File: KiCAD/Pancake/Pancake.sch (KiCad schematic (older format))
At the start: 44 parts, among them IC3 LF347N, J1 Conn_01x08_Male, J101 TB001-500-04BE, J102 TB001-500-03BE, J2 Conn_01x08_Male, J3 Conn_01x08_Male, J4 Conn_01x08_Male, J5 Conn_01x08_Male, J7 Conn_02x15_Top_Bottom

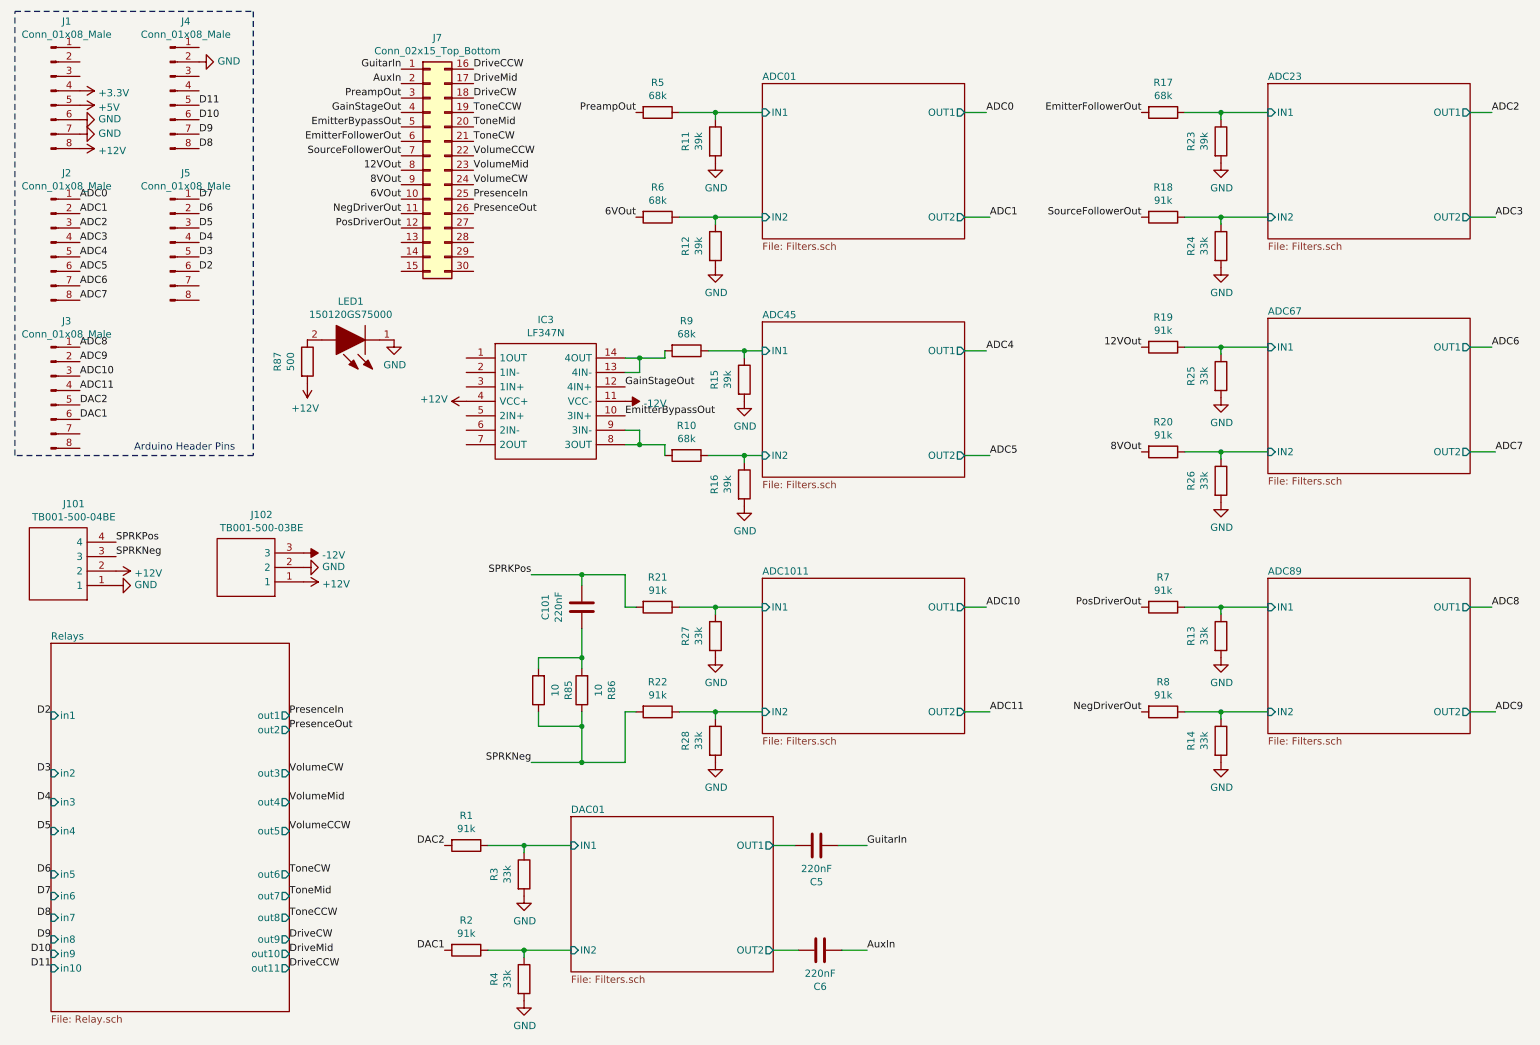
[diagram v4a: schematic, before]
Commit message: Will need to retrace in order to be built at SDSU.
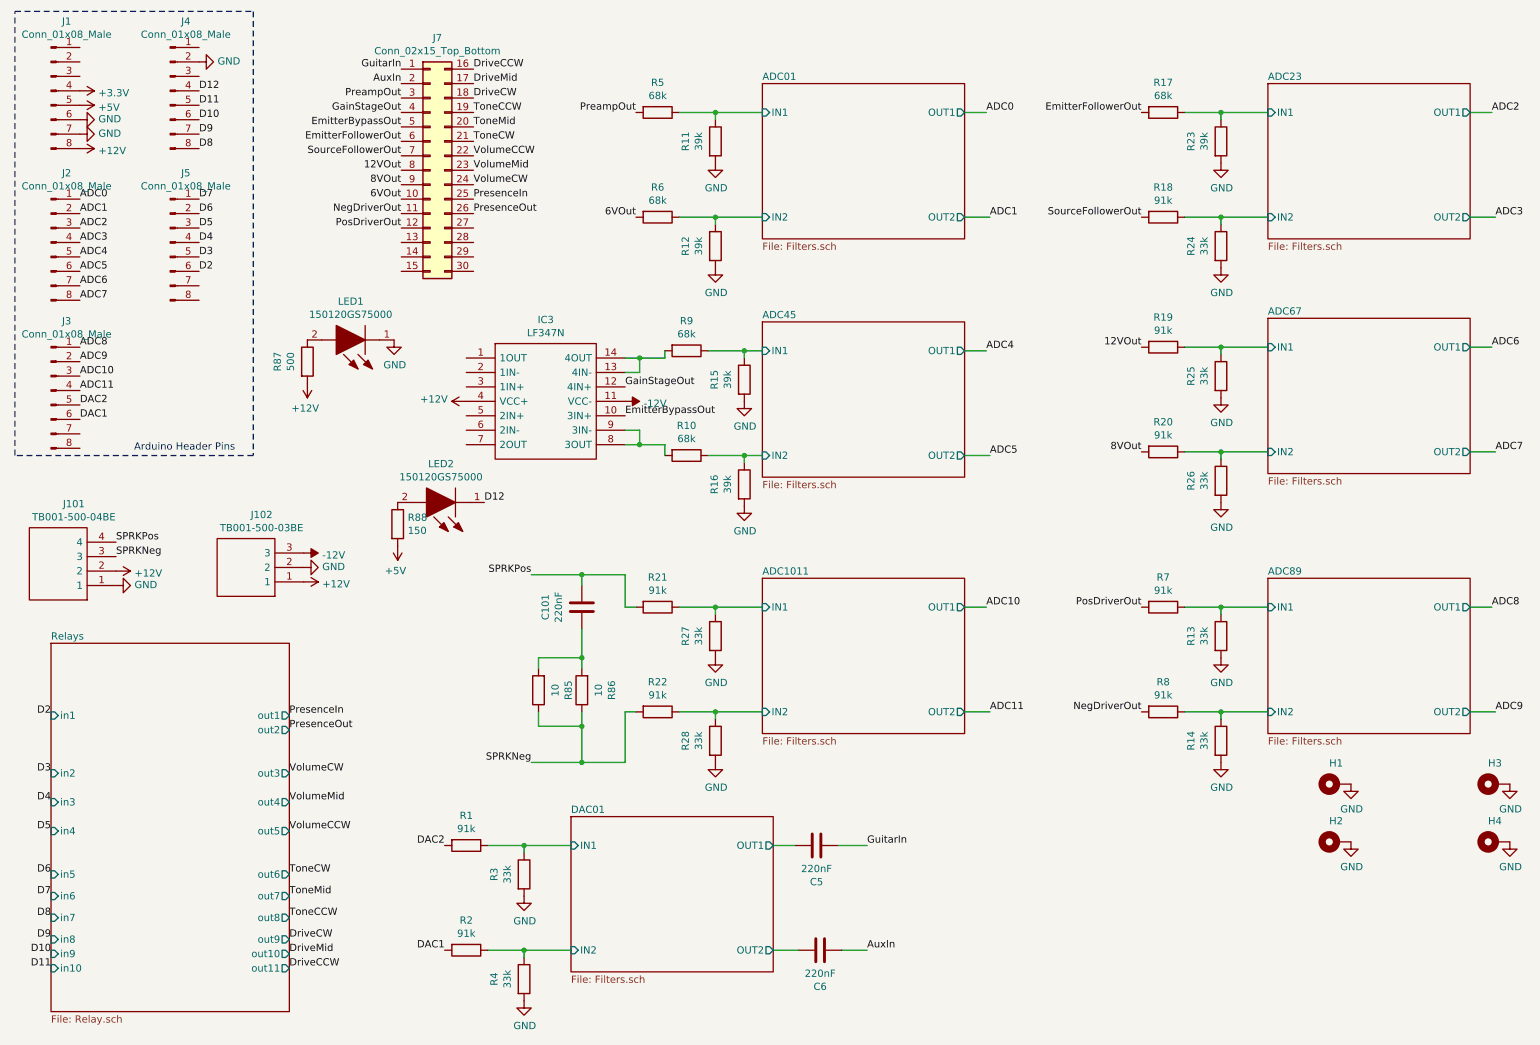
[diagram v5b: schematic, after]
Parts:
- added H1, H2, H3, H4: MountingHole_Pad, MountingHole:MountingHole_3.5mm_Pad_Via, symbol Mechanical:MountingHole_Pad
- added LED2: 150120GS75000, SamacSys_Parts:LEDC3214X78N, symbol SamacSys_Parts:150120GS75000
- added R88: 150, Resistor_SMD:R_1206_3216Metric_Pad1.30x1.75mm_HandSolder, symbol Device:R
- LED1: footprint LED_SMD:LED_1206_3216Metric -> SamacSys_Parts:LEDC3214X78N
- R87: footprint Resistor_THT:R_Axial_DIN0207_L6.3mm_D2.5mm_P10.16mm_Horizontal -> Resistor_SMD:R_1206_3216Metric_Pad1.30x1.75mm_HandSolder
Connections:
- net +5V: now also R88.2
- net GND: now also H1.1, H2.1, H3.1, H4.1
- net D12: now reaches J4.4 (Pin_4)
- net D12: now also LED2.1
- new net: LED2.2, R88.1
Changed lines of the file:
@@
 F 0 "LED1" H 3525 2583 50  0000 C CNN
 F 1 "150120GS75000" H 3525 2674 50  0000 C CNN
-F 2 "LED_SMD:LED_1206_3216Metric" H 3725 3000 50  0001 L BNN
+F 2 "SamacSys_Parts:LEDC3214X78N" H 3725 3000 50  0001 L BNN
 F 3 "https://docs-emea.rs-online.com/webdocs/1302/0900766b81302e28.pdf" H 3725 2900 50  0001 L BNN
 F 4 "LED,Wurth Elektronik,150120GS75000 Wurth Elektronik 150120GS75000, WL-SMCW Series Green LED, 520 nm, 3016 (1206) Clear, Rectangle Lens SMD Package" H 3725 2800 50  0001 L BNN "Description"
@@
 F 0 "R87" V 2418 3000 50  0000 C CNN
 F 1 "500" V 2509 3000 50  0000 C CNN
-F 2 "Resistor_THT:R_Axial_DIN0207_L6.3mm_D2.5mm_P10.16mm_Horizontal" V 2555 3000 50  0001 C CNN
+F 2 "Resistor_SMD:R_1206_3216Metric_Pad1.30x1.75mm_HandSolder" V 2555 3000 50  0001 C CNN
 F 3 "~" H 2625 3000 50  0001 C CNN
 	1    2625 3000
@@
 	1    0    0    -1
 $EndComp
+Text Label 1875 1125 0    50   ~ 0
+D12
+$Comp
+L Device:R R88
+U 1 1 6148EF40
+P 3250 4125
+F 0 "R88" H 3320 4171 50  0000 L CNN
+F 1 "150" H 3320 4080 50  0000 L CNN
+F 2 "Resistor_SMD:R_1206_3216Metric_Pad1.30x1.75mm_HandSolder" V 3180 4125 50  0001 C CNN
+F 3 "~" H 3250 4125 50  0001 C CNN
+	1    3250 4125
+	1    0    0    -1
+$EndComp
+$Comp
+L SamacSys_Parts:150120GS75000 LED2
+U 1 1 6148FA49
+P 3850 3975
+F 0 "LED2" H 4150 3708 50  0000 C CNN
+F 1 "150120GS75000" H 4150 3799 50  0000 C CNN
+F 2 "SamacSys_Parts:LEDC3214X78N" H 4350 4125 50  0001 L BNN
+F 3 "https://docs-emea.rs-online.com/webdocs/1302/0900766b81302e28.pdf" H 4350 4025 50  0001 L BNN
+F 4 "LED,Wurth Elektronik,150120GS75000 Wurth Elektronik 150120GS75000, WL-SMCW Series Green LED, 520 nm, 3016 (1206) Clear, Rectangle Lens SMD Package" H 4350 3925 50  0001 L BNN "Description"
+F 5 "0.78" H 4350 3825 50  0001 L BNN "Height"
+F 6 "Wurth Elektronik" H 4350 3725 50  0001 L BNN "Manufacturer_Name"
+F 7 "150120GS75000" H 4350 3625 50  0001 L BNN "Manufacturer_Part_Number"
+F 8 "710-150120GS75000" H 4350 3525 50  0001 L BNN "Mouser Part Number"
+F 9 "https://www.mouser.co.uk/ProductDetail/Wurth-Elektronik/150120GS75000?qs=LlUlMxKIyB3I3AMxrmBw4A%3D%3D" H 4350 3425 50  0001 L BNN "Mouser Price/Stock"
+F 10 "" H 4350 3325 50  0001 L BNN "Arrow Part Number"
+F 11 "" H 4350 3225 50  0001 L BNN "Arrow Price/Stock"
+	1    3850 3975
+	-1   0    0    1
+$EndComp
+Text Label 3850 3975 0    50   ~ 0
+D12
+$Comp
+L power:+5V #PWR03
+U 1 1 61490D1B
+P 3250 4275
+F 0 "#PWR03" H 3250 4125 50  0001 C CNN
+F 1 "+5V" H 3265 4448 50  0000 C CNN
+F 2 "" H 3250 4275 50  0001 C CNN
+F 3 "" H 3250 4275 50  0001 C CNN
+	1    3250 4275
+	-1   0    0    1
+$EndComp
+$Comp
+L Mechanical:MountingHole_Pad H4
+U 1 1 614F31BA
+P 10850 6325
+F 0 "H4" V 10995 6328 50  0000 C CNN
+F 1 "MountingHole_Pad" V 10996 6328 50  0001 C CNN
+F 2 "MountingHole:MountingHole_3.5mm_Pad_Via" H 10850 6325 50  0001 C CNN
+F 3 "~" H 10850 6325 50  0001 C CNN
+	1    10850 6325
+	0    -1   -1   0
+$EndComp
+$Comp
+L Mechanical:MountingHole_Pad H1
+U 1 1 614F33F8
+P 9750 5925
+F 0 "H1" V 9895 5928 50  0000 C CNN
+F 1 "MountingHole_Pad" V 9896 5928 50  0001 C CNN
+F 2 "MountingHole:MountingHole_3.5mm_Pad_Via" H 9750 5925 50  0001 C CNN
+F 3 "~" H 9750 5925 50  0001 C CNN
+	1    9750 5925
+	0    -1   -1   0
+$EndComp
+$Comp
+L Mechanical:MountingHole_Pad H3
+U 1 1 614F2F92
+P 10850 5925
+F 0 "H3" V 10995 5928 50  0000 C CNN
+F 1 "MountingHole_Pad" V 10996 5928 50  0001 C CNN
+F 2 "MountingHole:MountingHole_3.5mm_Pad_Via" H 10850 5925 50  0001 C CNN
+F 3 "~" H 10850 5925 50  0001 C CNN
+	1    10850 5925
+	0    -1   -1   0
+$EndComp
+$Comp
+L Mechanical:MountingHole_Pad H2
+U 1 1 614E9F86
+P 9750 6325
+F 0 "H2" V 9895 6328 50  0000 C CNN
+F 1 "MountingHole_Pad" V 9896 6328 50  0001 C CNN
+F 2 "MountingHole:MountingHole_3.5mm_Pad_Via" H 9750 6325 50  0001 C CNN
+F 3 "~" H 9750 6325 50  0001 C CNN
+	1    9750 6325
+	0    -1   -1   0
+$EndComp
+$Comp
+L power:GND #PWR04
+U 1 1 614F93B8
+P 9850 5925
+F 0 "#PWR04" H 9850 5675 50  0001 C CNN
+F 1 "GND" H 9855 5752 50  0000 C CNN
+F 2 "" H 9850 5925 50  0001 C CNN
+F 3 "" H 9850 5925 50  0001 C CNN
+	1    9850 5925
+	1    0    0    -1
+$EndComp
+$Comp
+L power:GND #PWR06
+U 1 1 614FA4A2
+P 10950 5925
+F 0 "#PWR06" H 10950 5675 50  0001 C CNN
+F 1 "GND" H 10955 5752 50  0000 C CNN
+F 2 "" H 10950 5925 50  0001 C CNN
+F 3 "" H 10950 5925 50  0001 C CNN
+	1    10950 5925
+	1    0    0    -1
+$EndComp
+$Comp
+L power:GND #PWR05
+U 1 1 614FABB2
+P 9850 6325
+F 0 "#PWR05" H 9850 6075 50  0001 C CNN
+F 1 "GND" H 9855 6152 50  0000 C CNN
+F 2 "" H 9850 6325 50  0001 C CNN
+F 3 "" H 9850 6325 50  0001 C CNN
+	1    9850 6325
+	1    0    0    -1
+$EndComp
+$Comp
+L power:GND #PWR07
+U 1 1 614FBC89
+P 10950 6325
+F 0 "#PWR07" H 10950 6075 50  0001 C CNN
+F 1 "GND" H 10955 6152 50  0000 C CNN
+F 2 "" H 10950 6325 50  0001 C CNN
+F 3 "" H 10950 6325 50  0001 C CNN
+	1    10950 6325
+	1    0    0    -1
+$EndComp

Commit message: Revising one last time before ordering
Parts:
- added R89: 1000, Resistor_SMD:R_1206_3216Metric_Pad1.30x1.75mm_HandSolder, symbol Device:R
- R87: value 500 -> 1000
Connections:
- net +12V: now also R87.1, R89.2; no longer R87.2
- net at LED1.2: now also R87.2, R89.1; no longer R87.1
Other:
- moved on the sheet: LED1, R87
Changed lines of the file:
@@
 L SamacSys_Parts:150120GS75000 LED1
 U 1 1 61471F94
-P 3225 2850
-F 0 "LED1" H 3525 2583 50  0000 C CNN
-F 1 "150120GS75000" H 3525 2674 50  0000 C CNN
-F 2 "SamacSys_Parts:LEDC3214X78N" H 3725 3000 50  0001 L BNN
-F 3 "https://docs-emea.rs-online.com/webdocs/1302/0900766b81302e28.pdf" H 3725 2900 50  0001 L BNN
-F 4 "LED,Wurth Elektronik,150120GS75000 Wurth Elektronik 150120GS75000, WL-SMCW Series Green LED, 520 nm, 3016 (1206) Clear, Rectangle Lens SMD Package" H 3725 2800 50  0001 L BNN "Description"
-F 5 "0.78" H 3725 2700 50  0001 L BNN "Height"
-F 6 "Wurth Elektronik" H 3725 2600 50  0001 L BNN "Manufacturer_Name"
-F 7 "150120GS75000" H 3725 2500 50  0001 L BNN "Manufacturer_Part_Number"
-F 8 "710-150120GS75000" H 3725 2400 50  0001 L BNN "Mouser Part Number"
-F 9 "https://www.mouser.co.uk/ProductDetail/Wurth-Elektronik/150120GS75000?qs=LlUlMxKIyB3I3AMxrmBw4A%3D%3D" H 3725 2300 50  0001 L BNN "Mouser Price/Stock"
-F 10 "" H 3725 2200 50  0001 L BNN "Arrow Part Number"
-F 11 "" H 3725 2100 50  0001 L BNN "Arrow Price/Stock"
-	1    3225 2850
+P 3425 2800
+F 0 "LED1" H 3725 2533 50  0000 C CNN
+F 1 "150120GS75000" H 3725 2624 50  0000 C CNN
+F 2 "SamacSys_Parts:LEDC3214X78N" H 3925 2950 50  0001 L BNN
+F 3 "https://docs-emea.rs-online.com/webdocs/1302/0900766b81302e28.pdf" H 3925 2850 50  0001 L BNN
+F 4 "LED,Wurth Elektronik,150120GS75000 Wurth Elektronik 150120GS75000, WL-SMCW Series Green LED, 520 nm, 3016 (1206) Clear, Rectangle Lens SMD Package" H 3925 2750 50  0001 L BNN "Description"
+F 5 "0.78" H 3925 2650 50  0001 L BNN "Height"
+F 6 "Wurth Elektronik" H 3925 2550 50  0001 L BNN "Manufacturer_Name"
+F 7 "150120GS75000" H 3925 2450 50  0001 L BNN "Manufacturer_Part_Number"
+F 8 "710-150120GS75000" H 3925 2350 50  0001 L BNN "Mouser Part Number"
+F 9 "https://www.mouser.co.uk/ProductDetail/Wurth-Elektronik/150120GS75000?qs=LlUlMxKIyB3I3AMxrmBw4A%3D%3D" H 3925 2250 50  0001 L BNN "Mouser Price/Stock"
+F 10 "" H 3925 2150 50  0001 L BNN "Arrow Part Number"
+F 11 "" H 3925 2050 50  0001 L BNN "Arrow Price/Stock"
+	1    3425 2800
 	-1   0    0    1
 $EndComp
@@
 L Device:R R?
 U 1 1 6147D62C
-P 2625 3000
+P 3000 3125
 AR Path="/61024B6A/6147D62C" Ref="R?"  Part="1"
 AR Path="/612AE90B/6147D62C" Ref="R?"  Part="1"
 AR Path="/6147D62C" Ref="R87"  Part="1"
-F 0 "R87" V 2418 3000 50  0000 C CNN
-F 1 "500" V 2509 3000 50  0000 C CNN
-F 2 "Resistor_SMD:R_1206_3216Metric_Pad1.30x1.75mm_HandSolder" V 2555 3000 50  0001 C CNN
-F 3 "~" H 2625 3000 50  0001 C CNN
-	1    2625 3000
-	1    0    0    -1
+F 0 "R87" V 2793 3125 50  0000 C CNN
+F 1 "1000" V 2884 3125 50  0000 C CNN
+F 2 "Resistor_SMD:R_1206_3216Metric_Pad1.30x1.75mm_HandSolder" V 2930 3125 50  0001 C CNN
+F 3 "~" H 3000 3125 50  0001 C CNN
+	1    3000 3125
+	-1   0    0    1
 $EndComp
 $Comp
 L power:+12V #PWR01
 U 1 1 61484A8A
-P 2625 3150
-F 0 "#PWR01" H 2625 3000 50  0001 C CNN
-F 1 "+12V" H 2640 3323 50  0000 C CNN
-F 2 "" H 2625 3150 50  0001 C CNN
-F 3 "" H 2625 3150 50  0001 C CNN
-	1    2625 3150
+P 2825 3300
+F 0 "#PWR01" H 2825 3150 50  0001 C CNN
+F 1 "+12V" H 2840 3473 50  0000 C CNN
+F 2 "" H 2825 3300 50  0001 C CNN
+F 3 "" H 2825 3300 50  0001 C CNN
+	1    2825 3300
 	-1   0    0    1
 $EndComp
@@
 L power:GND #PWR02
 U 1 1 61485A09
-P 3225 2850
-F 0 "#PWR02" H 3225 2600 50  0001 C CNN
-F 1 "GND" H 3230 2677 50  0000 C CNN
-F 2 "" H 3225 2850 50  0001 C CNN
-F 3 "" H 3225 2850 50  0001 C CNN
-	1    3225 2850
+P 3425 2800
+F 0 "#PWR02" H 3425 2550 50  0001 C CNN
+F 1 "GND" H 3430 2627 50  0000 C CNN
+F 2 "" H 3425 2800 50  0001 C CNN
+F 3 "" H 3425 2800 50  0001 C CNN
+	1    3425 2800
 	1    0    0    -1
 $EndComp
@@
 	1    0    0    -1
 $EndComp
+$Comp
+L Device:R R?
+U 1 1 614E4DCA
+P 2625 3125
+AR Path="/61024B6A/614E4DCA" Ref="R?"  Part="1"
+AR Path="/612AE90B/614E4DCA" Ref="R?"  Part="1"
+AR Path="/614E4DCA" Ref="R89"  Part="1"
+F 0 "R89" V 2418 3125 50  0000 C CNN
+F 1 "1000" V 2509 3125 50  0000 C CNN
+F 2 "Resistor_SMD:R_1206_3216Metric_Pad1.30x1.75mm_HandSolder" V 2555 3125 50  0001 C CNN
+F 3 "~" H 2625 3125 50  0001 C CNN
+	1    2625 3125
+	1    0    0    -1
+$EndComp
+Wire Wire Line
+	2825 3300 2825 3275
+Wire Wire Line
+	2825 3275 3000 3275
+Wire Wire Line
+	2625 3275 2825 3275
+Connection ~ 2825 3275
+Wire Wire Line
+	2625 2975 2825 2975
+Wire Wire Line
+	2825 2800 2825 2975
+Connection ~ 2825 2975
+Wire Wire Line
+	2825 2975 3000 2975
 $EndSCHEMATC

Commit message: PDF Outputs
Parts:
- LED1, LED2: symbol SamacSys_Parts:150120GS75000 -> Pancake-rescue:150120GS75000-SamacSys_Parts
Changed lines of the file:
@@
 encoding utf-8
 Sheet 1 9
-Title ""
-Date ""
-Rev ""
-Comp ""
+Title "Pancake Test Fixture"
+Date "2021-09-26"
+Rev "A"
+Comp "San Diego State University"
 Comment1 ""
 Comment2 ""
@@
 	4525 5525 4525 5775
 $Comp
-L SamacSys_Parts:150120GS75000 LED1
+L Pancake-rescue:150120GS75000-SamacSys_Parts LED1
 U 1 1 61471F94
 P 3425 2800
@@
 $EndComp
 $Comp
-L SamacSys_Parts:150120GS75000 LED2
+L Pancake-rescue:150120GS75000-SamacSys_Parts LED2
 U 1 1 6148FA49
 P 3850 3975
